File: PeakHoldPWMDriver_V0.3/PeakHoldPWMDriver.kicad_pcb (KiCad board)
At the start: 2 copper layers, 100.1 x 50 mm, 105 parts, among them J1 Screw_Terminal_01x06, J2 Screw_Terminal_01x08, Q1 AO3400, Q10 AO3400, Q11 2N7002, Q12 2N7002, Q13 TSM2309, Q14 IRLL 024N, Q15 TSM2309, Q16 IRLL 024N, Q2 AO3400, Q3 2N7002, Q4 2N7002, Q5 TSM2309, Q6 TSM2309, Q7 IRLL 024N, Q8 IRLL 024N, Q9 AO3400, U1 74LS32, U2 LM2901, U3 74LS74, U4 LTC6992, U5 74LS74, U6 LM78M05, U7 74LS08, U8 74LS08

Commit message: cleaup
cleanup of silkscreen
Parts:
- R3: value 500k -> 470k
- moved RV2 0.25 mm to (194.3, 69.1)
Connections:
- RV1 pad 1: Net-(D1-Pad2) -> PWR_GND
- RV1 pad 3: PWR_GND -> Net-(D1-Pad2)
- RV2 pad 1: Net-(D4-Pad2) -> PWR_GND
- RV2 pad 3: PWR_GND -> Net-(D4-Pad2)
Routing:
- net PWR_GND: track 545.6 -> 535.3 mm, vias 110 -> 107
- net Net-(D1-Pad2): track 12.0 -> 7.60 mm
- net Net-(D4-Pad2): track 5.64 -> 9.71 mm

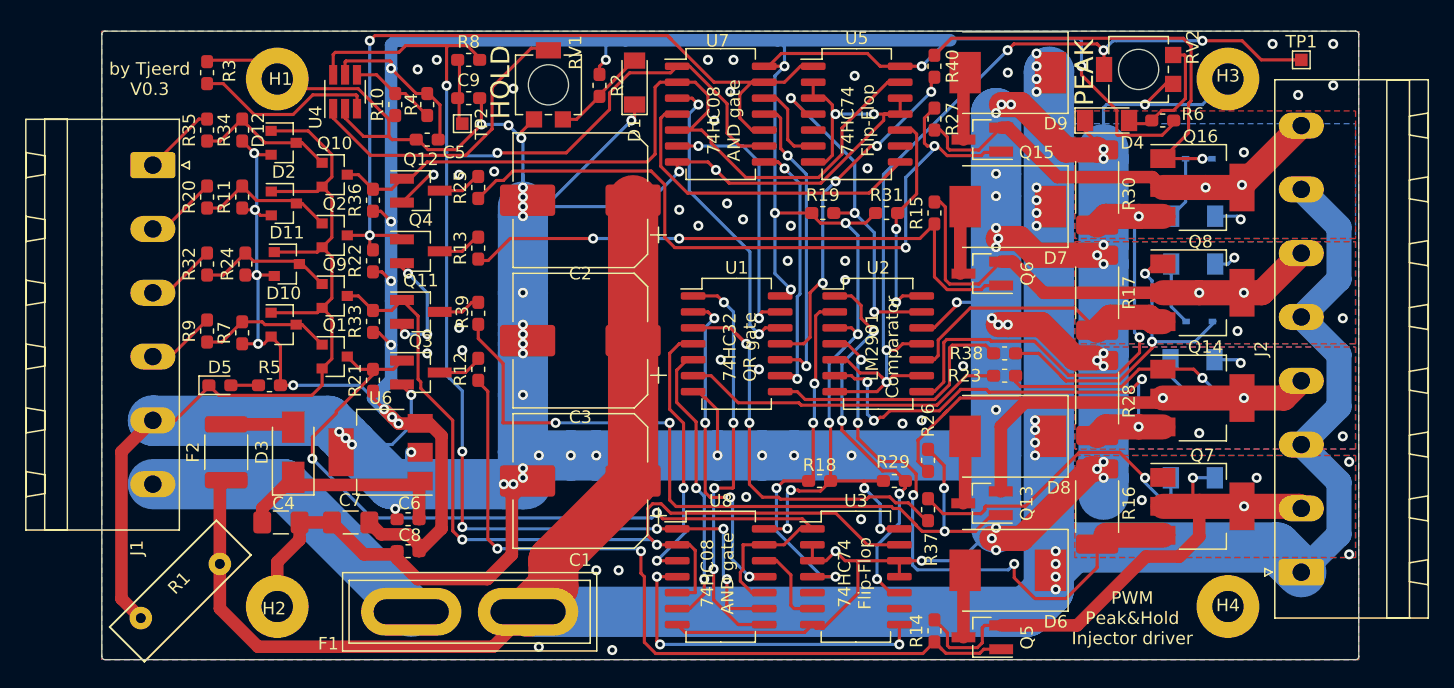
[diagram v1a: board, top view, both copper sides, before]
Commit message: Added jumpers to choose between ECU or transistor input
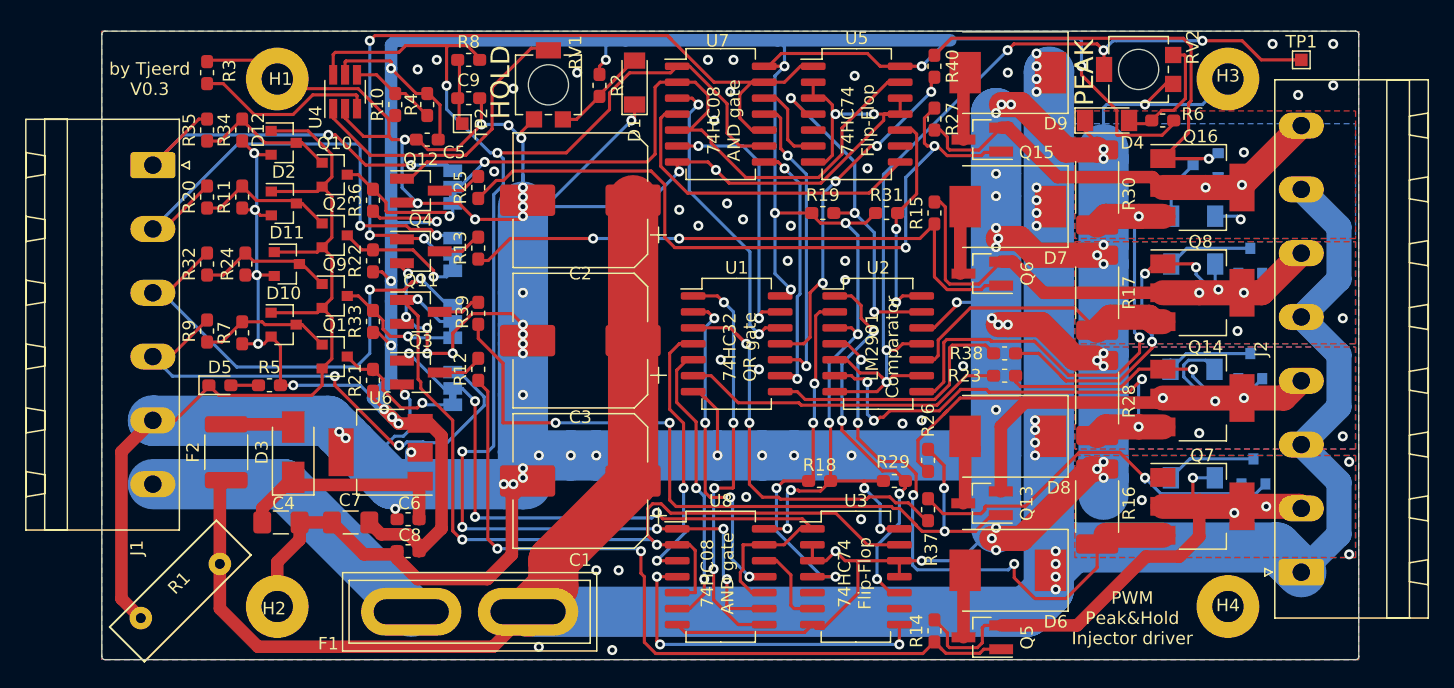
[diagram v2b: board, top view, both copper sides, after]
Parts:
- added JP1: SolderJumper_3_Bridged12, Jumper:SolderJumper-3_P1.3mm_Bridged12_Pad1.0x1.5mm, B.Cu at (139.7, 94.5)
- added JP2: SolderJumper_3_Bridged12, Jumper:SolderJumper-3_P1.3mm_Bridged12_Pad1.0x1.5mm, B.Cu at (139.7, 83.8)
- added JP3: SolderJumper_3_Bridged12, Jumper:SolderJumper-3_P1.3mm_Bridged12_Pad1.0x1.5mm, B.Cu at (139.7, 89.2)
- added JP4: SolderJumper_3_Bridged12, Jumper:SolderJumper-3_P1.3mm_Bridged12_Pad1.0x1.5mm, B.Cu at (139.7, 78.5)
- D13, D14, D17, D18: value MM3Z47V -> BZX84C56; footprint Diode_SMD:D_SOD-323 -> Diode_SMD:D_SOT-23_ANK
- moved D14 6.31 mm to (203.2, 84.3), turned to 90 degrees
- moved D13 5.29 mm to (203.5, 101.1), turned to 90 degrees
- moved D17 4.54 mm to (203.2, 92.7), turned to 90 degrees
- moved D19 0.76 mm to (198.6, 93.0)
- moved D18 0.74 mm to (199.6, 76.7), turned to 180 degrees
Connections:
- Q1 pad 3: inv_INJ1 -> Net-(JP1-Pad1)
- Q10 pad 3: inv_INJ4 -> Net-(JP4-Pad1)
- Q2 pad 3: inv_INJ3 -> Net-(JP2-Pad1)
- Q9 pad 3: inv_INJ2 -> Net-(JP3-Pad1)
- R21 pad 2: inv_INJ1 -> Net-(JP1-Pad1)
- R22 pad 2: inv_INJ3 -> Net-(JP2-Pad1)
- R33 pad 2: inv_INJ2 -> Net-(JP3-Pad1)
- R36 pad 2: inv_INJ4 -> Net-(JP4-Pad1)
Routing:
- net INJ1: track 5.52 -> 43.2 mm, vias 0 -> 2
- net INJ3: track 5.73 -> 39.2 mm, vias 0 -> 2
- net INJ2: track 5.63 -> 38.8 mm, vias 0 -> 2
- net INJ4: track 5.84 -> 31.9 mm, vias 0 -> 2
- net PWR_GND: track 535.3 -> 557.4 mm
- net inv_INJ1: track 68.2 -> 56.3 mm, vias 2 -> 4
- net Net-(JP1-Pad1): track 0.00 -> 11.2 mm, vias 0 -> 1
- net Net-(JP4-Pad1): track 0.00 -> 11.0 mm, vias 0 -> 1
- net Net-(JP2-Pad1): track 0.00 -> 10.6 mm, vias 0 -> 1
- net Net-(JP3-Pad1): track 0.00 -> 10.2 mm, vias 0 -> 1
- net 5V: track 274.8 -> 281.7 mm
- net Net-(D14-Pad2): track 27.0 -> 33.0 mm, vias 2 -> 3
- net Net-(D17-Pad1): track 3.05 -> 8.17 mm
- net INJ2-OUT: track 46.0 -> 51.0 mm
- net Net-(D17-Pad2): track 17.8 -> 22.3 mm
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
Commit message: clean-up pcb
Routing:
- net INJ2-OUT: track 51.0 -> 52.3 mm
- net Net-(Q7-Pad3): track 46.4 -> 45.1 mm
- net Net-(Q15-Pad1): track 59.2 -> 60.3 mm
- net PWR_GND: track 557.4 -> 558.2 mm
- net Net-(JP2-Pad1): track 10.6 -> 9.93 mm

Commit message: Updates on V0.3
Updated V0.3
- Created readme
- Cleaned up baord.
- Created gerbers
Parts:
- Q1, Q10, Q2, Q9: value AO3400 -> 2N7002
- Q11, Q12, Q3, Q4: footprint Package_TO_SOT_SMD:SOT-23_Handsoldering -> Package_TO_SOT_SMD:SOT-23
- renumbered D14 to D10, D6 to D11, D7 to D12, D11 to D13, D12 to D14, D19 to D15, D17 to D16, D20 to D17, D8 to D19, D3 to D2, D9 to D20, D4 to D3, D5 to D4, D10 to D5, D2 to D6, D15 to D7, D13 to D8, D16 to D9, R2 to R1, R8 to R10, R20 to R12, R21 to R13, R22 to R14, R12 to R15, R13 to R16, R14 to R17, R37 to R18, R15 to R19, R1 to R2, R38 to R20, R16 to R21, R17 to R22, R18 to R23, R19 to R24, R24 to R25, R32 to R26, R33 to R27, R34 to R28, R35 to R29, R36 to R30, R39 to R31, R25 to R32, R23 to R33, R26 to R34, R27 to R35, R40 to R36, R28 to R37, R30 to R38, R29 to R39, R10 to R4, R31 to R40, R4 to R5, R5 to R6, R6 to R7, R7 to R8
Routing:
- net INJ3-OUT: track 40.5 -> 50.2 mm
- net PWM: track 116.2 -> 119.4 mm
- net Net-(U1-Pad5): track 23.0 -> 24.9 mm
- net Net-(U1-Pad1): track 33.3 -> 31.5 mm
- net VREF: track 73.7 -> 72.0 mm, vias 5 -> 4
- net Net-(D8-Pad2): track 33.0 -> 34.2 mm
- net inv_INJ2: track 74.4 -> 73.3 mm
- net Net-(U3-Pad8): track 27.8 -> 28.6 mm, vias 3 -> 2
- net Net-(Q4-Pad3): track 3.24 -> 4.04 mm
- net Net-(Q12-Pad3): track 3.24 -> 4.04 mm
- net Net-(U1-Pad4): track 22.2 -> 23.0 mm
- net Net-(U1-Pad2): track 26.8 -> 27.5 mm
- net 5V: track 281.7 -> 282.4 mm
- net Net-(Q5-Pad1): track 63.4 -> 64.1 mm
- net Net-(Q8-Pad3): track 22.9 -> 23.6 mm
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
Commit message: Added supplier to BOM list
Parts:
- J1: value Screw_Terminal_01x06 -> RND 205-00203
- J2: value Screw_Terminal_01x08 -> RND 205-00205

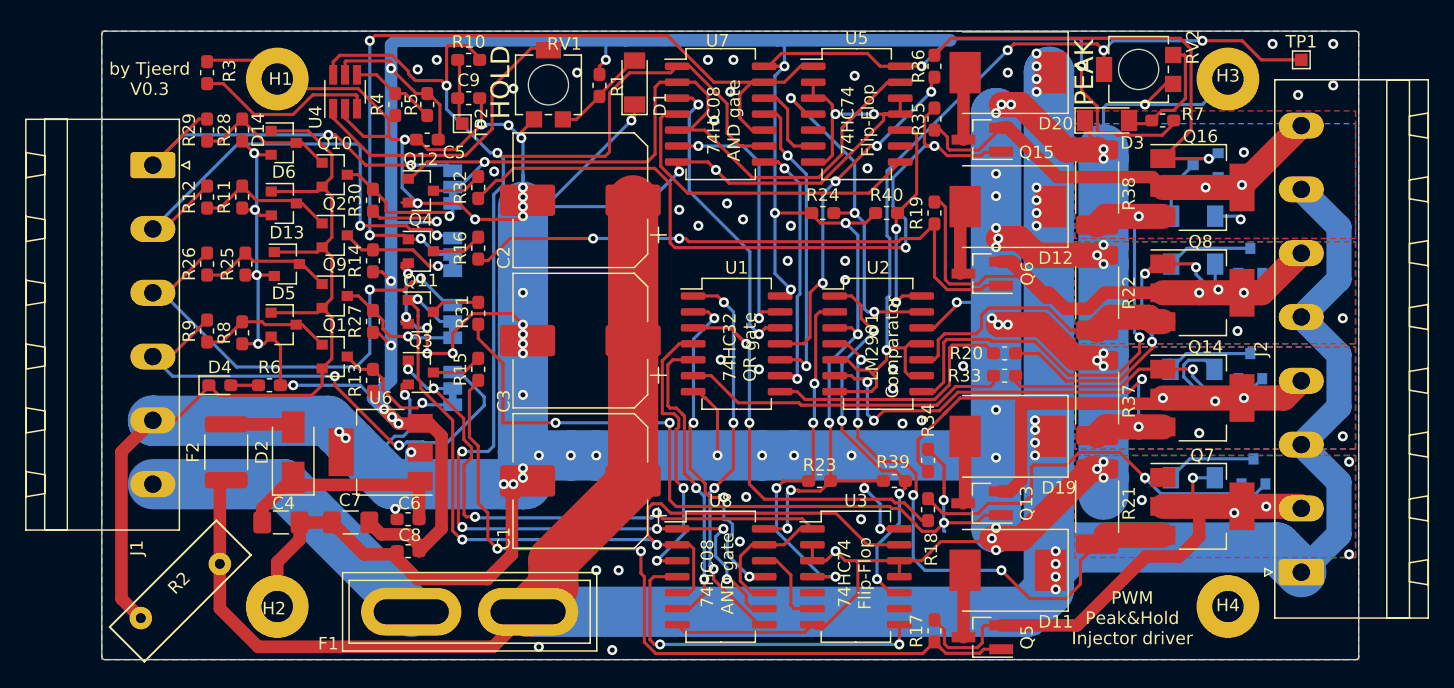
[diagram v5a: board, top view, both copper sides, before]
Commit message: Update V0.3 PCB
Updated V0.3 pcb with pulldown resistors when using ECU input. And some Cleanup pcb
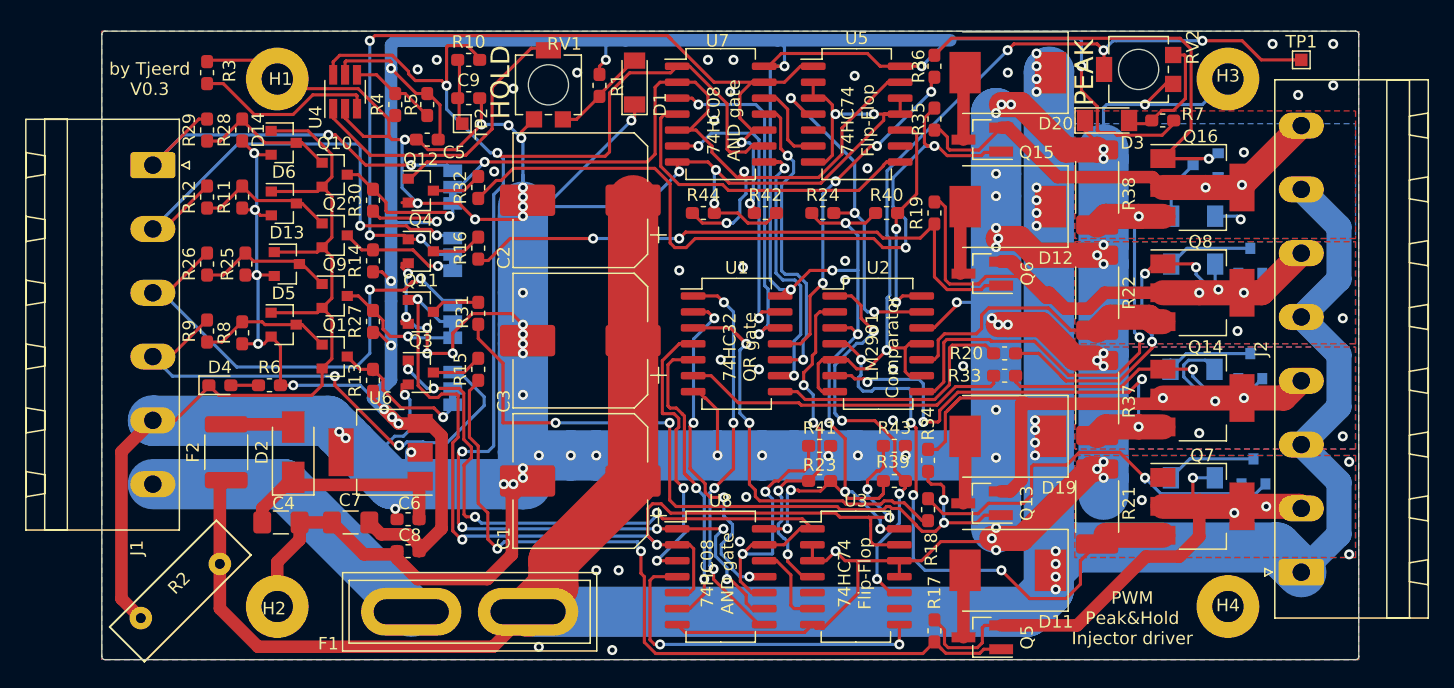
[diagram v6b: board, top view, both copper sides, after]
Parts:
- added R41: 1K, Resistor_SMD:R_0603_1608Metric_Pad1.05x0.95mm_HandSolder, F.Cu at (168.9, 99.1)
- added R42: 1K, Resistor_SMD:R_0603_1608Metric_Pad1.05x0.95mm_HandSolder, F.Cu at (164.6, 80.5)
- added R43: 1K, Resistor_SMD:R_0603_1608Metric_Pad1.05x0.95mm_HandSolder, F.Cu at (174.9, 99.1)
- added R44: 1K, Resistor_SMD:R_0603_1608Metric_Pad1.05x0.95mm_HandSolder, F.Cu at (159.7, 80.5)
- U6: value LM78M05 -> LM340
- turned R34 to 90 degrees
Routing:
- net inv_INJ1: track 56.8 -> 71.7 mm, vias 4 -> 6
- net inv_INJ2: track 73.3 -> 85.1 mm, vias 3 -> 5
- net PWR_GND: track 558.2 -> 569.3 mm, vias 110 -> 105
- net 5V: track 282.4 -> 291.9 mm
- net inv_INJ4: track 61.8 -> 71.1 mm, vias 1 -> 3
- net inv_INJ3: track 67.6 -> 76.4 mm, vias 3 -> 5
- net Net-(U1-Pad12): track 24.7 -> 27.4 mm
- net Net-(U1-Pad9): track 20.7 -> 23.0 mm
- net Net-(Q13-Pad1): track 63.2 -> 61.3 mm
- net Net-(U1-Pad13): track 21.5 -> 23.4 mm
- net Net-(R23-Pad2): track 29.3 -> 27.5 mm
- net Net-(R39-Pad2): track 32.2 -> 33.8 mm
- net Net-(Q7-Pad3): track 45.0 -> 46.5 mm
- net PWM: track 119.4 -> 120.5 mm
- net Net-(R18-Pad2): track 32.5 -> 33.5 mm
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
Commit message: Update zener value
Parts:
- D10, D16, D18, D8: value BZX84C56 -> BZX84C39

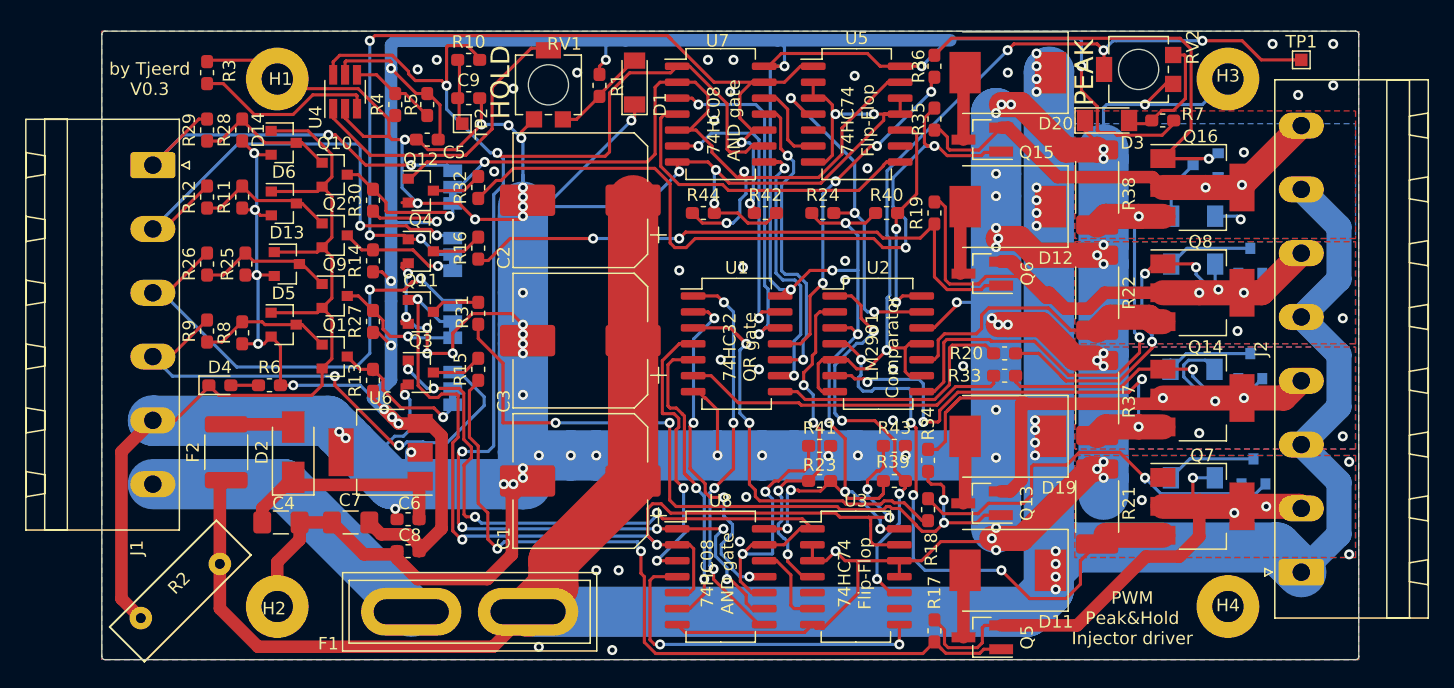
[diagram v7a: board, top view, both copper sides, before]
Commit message: update on p-chan mosfets
Overheating issues hopefully solved by this mod
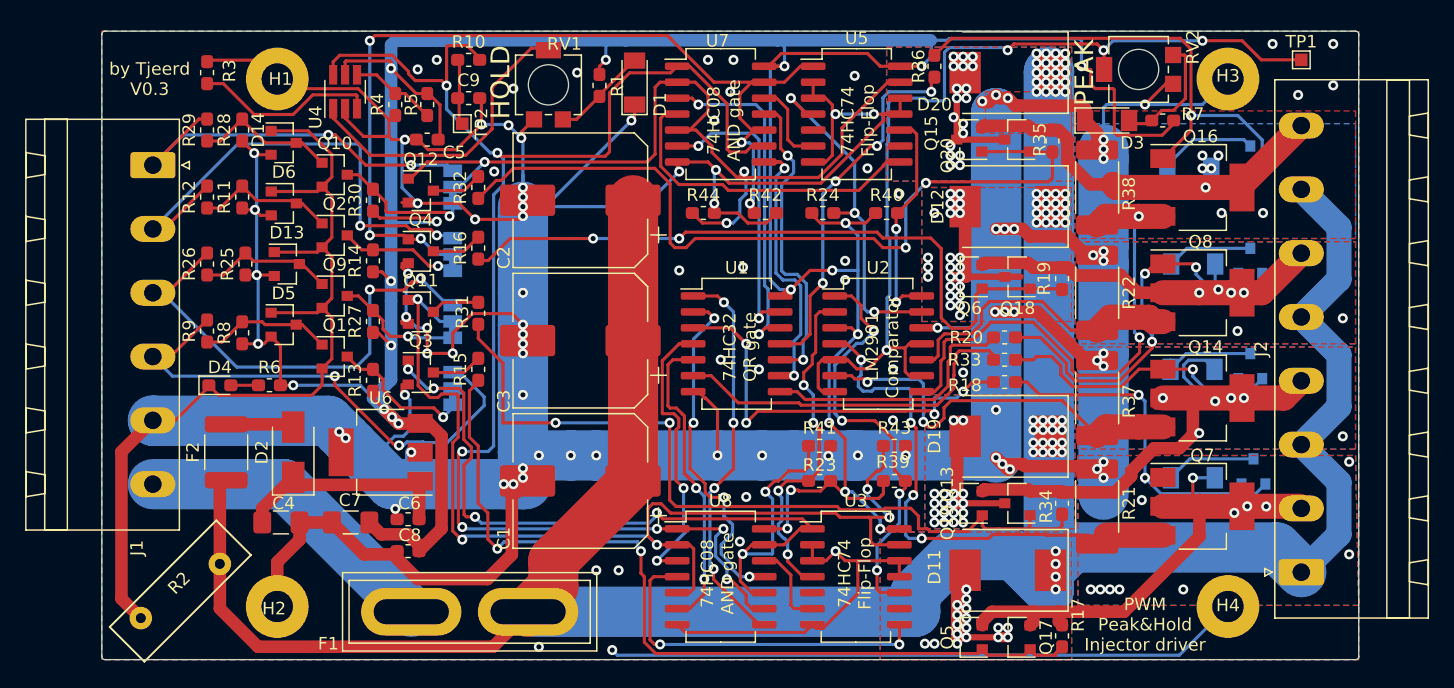
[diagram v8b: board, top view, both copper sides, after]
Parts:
- added Q17: TSM2309, Package_TO_SOT_SMD:SOT-23, F.Cu at (184.7, 114.3)
- added Q18: TSM2309, Package_TO_SOT_SMD:SOT-23, F.Cu at (184.7, 85.6)
- added Q19: TSM2309, Package_TO_SOT_SMD:SOT-23, F.Cu at (184.7, 103.6)
- added Q20: TSM2309, Package_TO_SOT_SMD:SOT-23, F.Cu at (184.6, 74.7)
- Q13, Q15, Q5, Q6: footprint Package_TO_SOT_SMD:SOT-23_Handsoldering -> Package_TO_SOT_SMD:SOT-23
- R15, R16, R31, R32: value 1K8 -> 470R
- moved R18 11.8 mm to (183.6, 94.0), turned to 180 degrees
- moved R19 11.4 mm to (188.2, 85.7)
- moved R34 11.2 mm to (188.2, 103.6)
- moved R17 10.2 mm to (188.2, 114.2)
- moved R35 9.56 mm to (187.5, 74.8), turned to 90 degrees
- moved D17 3.82 mm to (198.3, 77.0)
- moved D18 3.59 mm to (203.2, 76.2), turned to 90 degrees
- moved R20 1.27 mm to (183.6, 90.4)
- moved R33 1.27 mm to (183.6, 92.2)
- moved Q15 1.03 mm to (180.8, 74.7)
- moved Q6 1.03 mm to (180.9, 85.6)
- moved Q5 1.00 mm to (180.9, 114.3)
- moved Q13 0.98 mm to (180.9, 103.6)
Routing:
- net PWR_GND: track 569.3 -> 605.0 mm, vias 105 -> 103
- net INJ3-OUT: track 50.2 -> 30.0 mm, vias 5 -> 6
- net INJ2-OUT: track 51.3 -> 41.9 mm, vias 5 -> 6
- net Net-(Q18-Pad1): track 48.2 -> 56.6 mm
- net VREF: track 71.4 -> 77.1 mm
- net INJ4-OUT: track 37.4 -> 32.4 mm, vias 4 -> 7
- net Net-(D8-Pad2): track 34.2 -> 29.3 mm, vias 1 -> 2
- net Net-(Q7-Pad3): track 46.5 -> 41.8 mm
- net Net-(D12-Pad2): track 5.49 -> 9.95 mm, vias 0 -> 23
- net Net-(D20-Pad2): track 5.39 -> 9.80 mm, vias 0 -> 18
- net Net-(Q17-Pad1): track 64.7 -> 69.0 mm
- net INJ1-OUT: track 44.8 -> 40.5 mm, vias 6 -> 12
- net Net-(D11-Pad2): track 5.39 -> 9.59 mm, vias 0 -> 17
- net Net-(D19-Pad2): track 6.09 -> 10.1 mm, vias 0 -> 18
- net Net-(Q14-Pad3): track 39.3 -> 35.3 mm, vias 4 -> 2
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- added copper zone on B.Cu, net Net-(D11-Pad2)
- added copper zone on F.Cu, net Net-(D11-Pad2)
- added copper zone on B.Cu, net Net-(D12-Pad2)
- added copper zone on F.Cu, net Net-(D12-Pad2)
- added copper zone on B.Cu, net Net-(D19-Pad2)
- added copper zone on F.Cu, net Net-(D19-Pad2)
- added copper zone on B.Cu, net Net-(D20-Pad2)
- added copper zone on F.Cu, net Net-(D20-Pad2)
